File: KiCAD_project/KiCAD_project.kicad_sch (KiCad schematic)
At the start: 17 parts, among them SW1 SW_Push, SW10 RotaryEncoder_Switch, SW2 SW_Push, SW3 SW_Push, SW4 SW_Push, SW5 SW_Push, SW6 SW_Push, SW7 SW_Push, SW8 SW_Push, SW9 SW_Push, U1 XIAO-RP2040-DIP

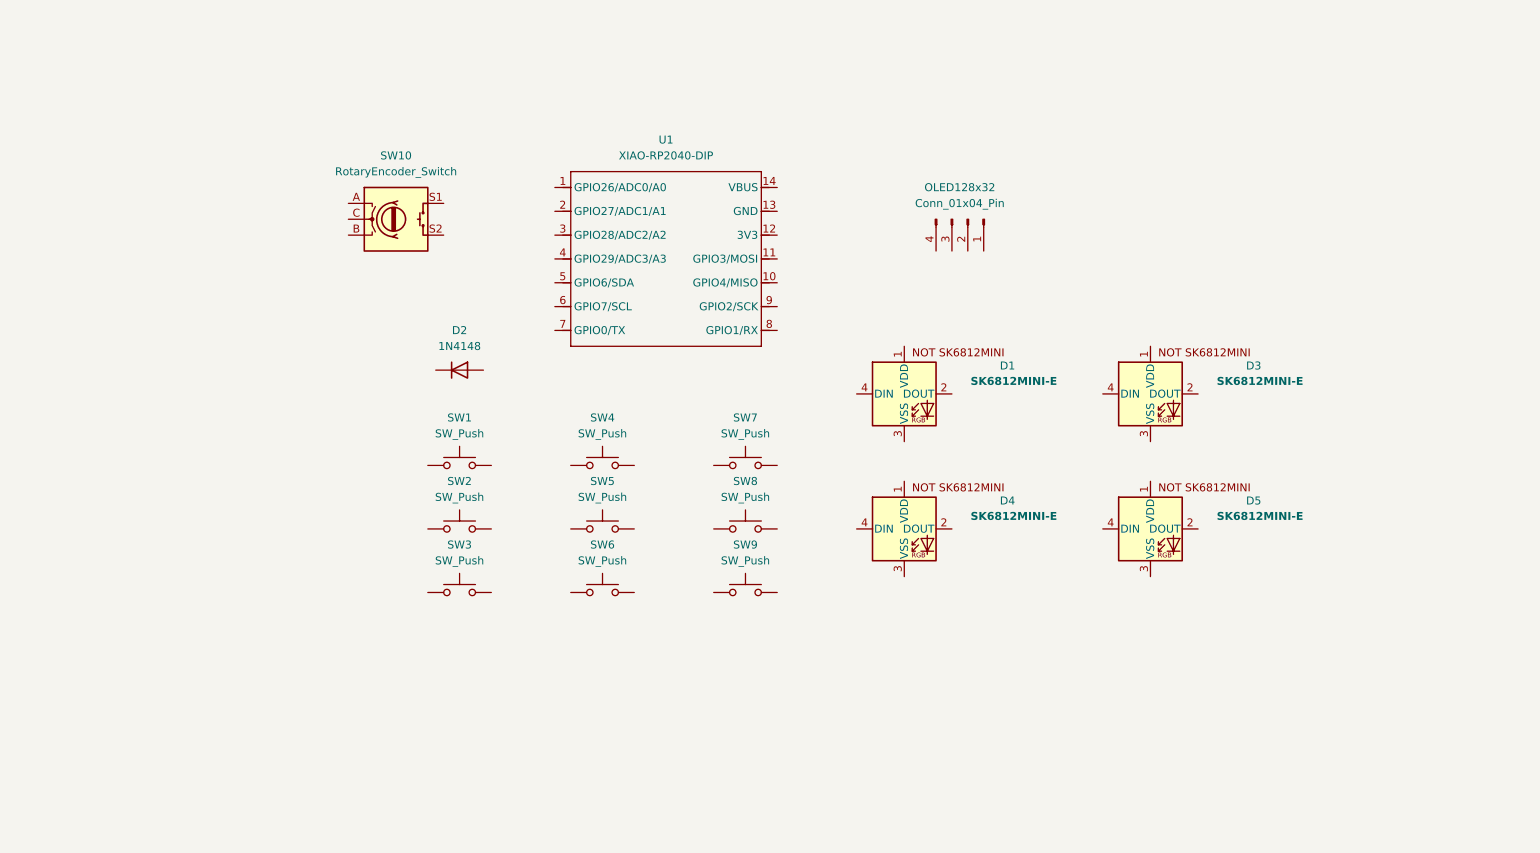
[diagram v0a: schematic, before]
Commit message: added images and BOM into readme.md
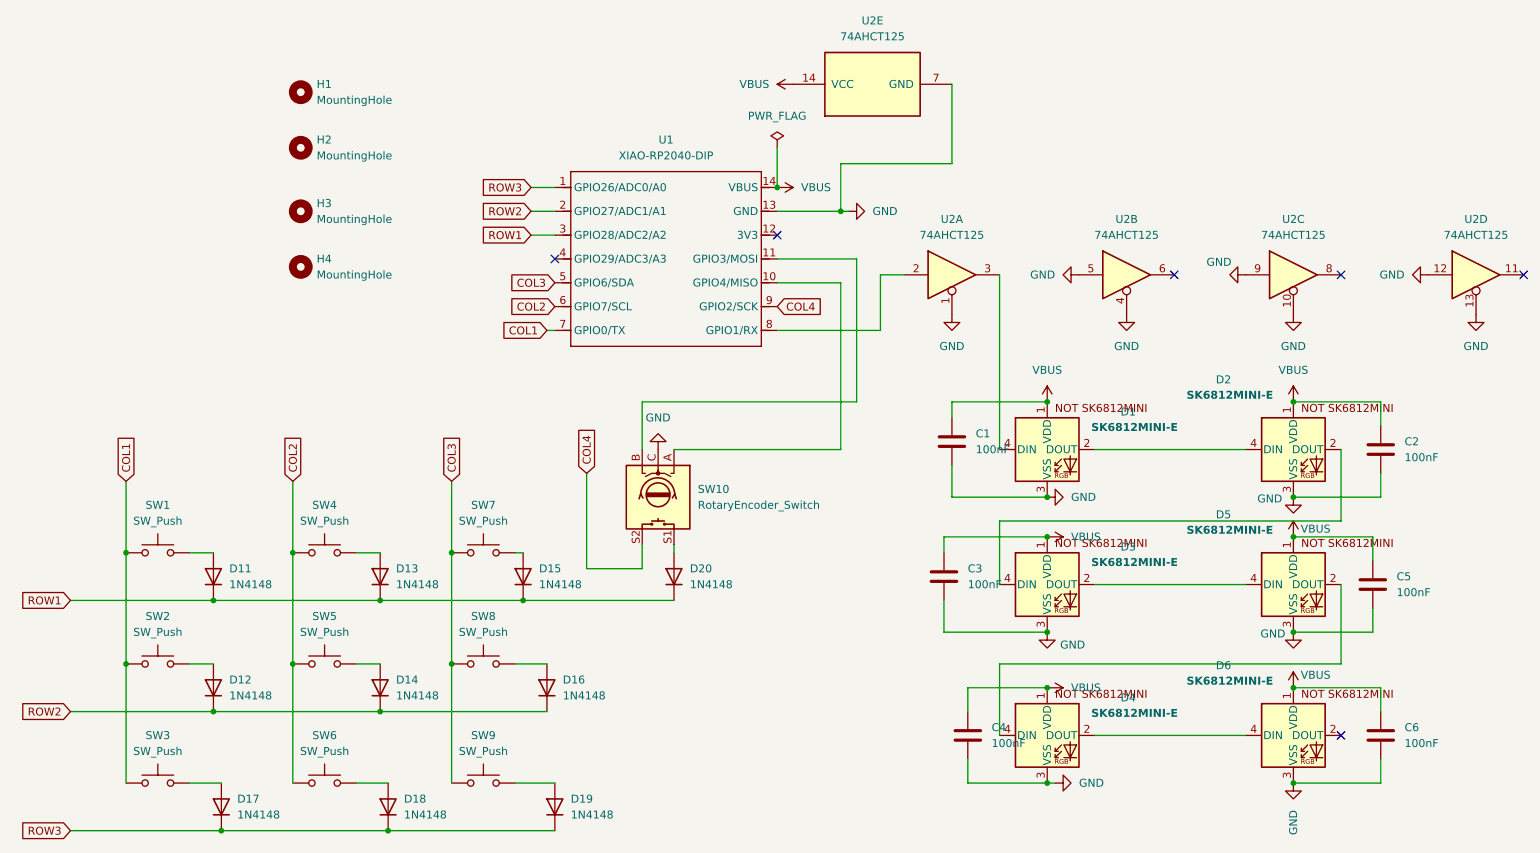
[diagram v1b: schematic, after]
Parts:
- removed OLED128x32: Conn_01x04_Pin, Connector_PinHeader_2.54mm:PinHeader_1x04_P2.54mm_Vertical, symbol Connector:Conn_01x04_Pin
- added C1, C2, C3, C4, C5, C6: 100nF, Capacitor_SMD:C_0603_1608Metric, symbol Device:C
- added D12, D13, D14, D15, D16, D17, D18, D19, D20: 1N4148, Diode_THT:D_DO-35_SOD27_P7.62mm_Horizontal, symbol Diode:1N4148
- added D4, D6: SK6812MINI-E, footprints:SK6812MINI-E_fixed, symbol SK6812MINI-E:SK6812MINI-E
- added H1, H2, H3, H4: MountingHole, MountingHole:MountingHole_3.2mm_M3, symbol Mechanical:MountingHole
- added U2: 74AHCT125, Package_DIP:DIP-14_W7.62mm, symbol 74xx:74AHCT125
- renumbered D2 to D11, D3 to D2, D4 to D3
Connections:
- net COL2: now reaches SW6.1
- net COL2: now also SW4.1, SW5.1, U1.6 (GPIO7/SCL)
- net at SW6.2: now also D18.2 (A)
- net COL3: now reaches SW7.1
- net COL3: now also SW8.1, SW9.1, U1.5 (GPIO6/SDA)
- net at SW7.2: now also D15.2 (A)
- net at SW9.2: now also D19.2 (A)
- net at SW5.2: now also D14.2 (A)
- net COL1: now reaches SW3.1
- net COL1: now also SW1.1, SW2.1, U1.7 (GPIO0/TX)
- net at SW3.2: now also D17.2 (A)
- net at SW4.2: now also D13.2 (A)
- net at SW8.2: now also D16.2 (A)
- net VBUS: now reaches D2.1 (VDD)
- net VBUS: now also D1.1 (VDD), D3.1 (VDD), D5.1 (VDD), U1.14 (VBUS), C1.1, C2.1, C3.1, C4.1, C5.1, C6.1, D4.1 (VDD), D6.1 (VDD), U2.14 (VCC)
- net at D2.2 (DOUT): now also D3.4 (DIN)
- net GND: now reaches D2.3 (VSS)
- net GND: now also D1.3 (VSS), D3.3 (VSS), D5.3 (VSS), SW10.C, U1.13 (GND), C1.2, C2.2, C3.2, C4.2, C5.2, C6.2, D4.3 (VSS), D6.3 (VSS), U2.1, U2.10, U2.12, U2.13, U2.4, U2.5, U2.7 (GND), U2.9
- net at D2.4 (DIN): now also D1.2 (DOUT)
- net at SW2.2: now also D12.2 (A)
- net ROW3: now reaches U1.1 (GPIO26/ADC0/A0)
- net ROW3: now also D17.1 (K), D18.1 (K), D19.1 (K)
- net at U1.10 (GPIO4/MISO): now also SW10.A
- net at U1.11 (GPIO3/MOSI): now also SW10.B
- net ROW2: now reaches U1.2 (GPIO27/ADC1/A1)
- net ROW2: now also D12.1 (K), D14.1 (K), D16.1 (K)
- net ROW1: now reaches U1.3 (GPIO28/ADC2/A2)
- net ROW1: now also D11.1 (K), D13.1 (K), D15.1 (K), D20.1 (K)
- net at U1.8 (GPIO1/RX): now also U2.2
- net COL4: now reaches U1.9 (GPIO2/SCK)
- net COL4: now also SW10.S2
- net at SW1.2: now also D11.2 (A)
- net at D5.2 (DOUT): now also D4.4 (DIN)
- net at D5.4 (DIN): now also D3.2 (DOUT)
- net at SW10.S1: now also D20.2 (A)
- net at D1.4 (DIN): now also U2.3
- new net: D4.2 (DOUT), D6.4 (DIN)
- no-connect marks 0 -> 6
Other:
- moved on the sheet: D1, D11, D2, D3, D5, SW1, SW10, SW2, SW3, SW4, SW5, SW6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
